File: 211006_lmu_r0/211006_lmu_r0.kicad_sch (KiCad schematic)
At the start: 17 parts, among them J1 Conn_02x03_Odd_Even, J14 Conn_01x02, J15 Conn_01x02, J16 Conn_01x02, J17 Conn_01x02, J18 Conn_01x02, J19 Conn_01x02, J2 Conn_02x03_Odd_Even, J20 Conn_01x02, J21 Conn_01x02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

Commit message: little bit closer
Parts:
- gave numbers to parts that had none: 1

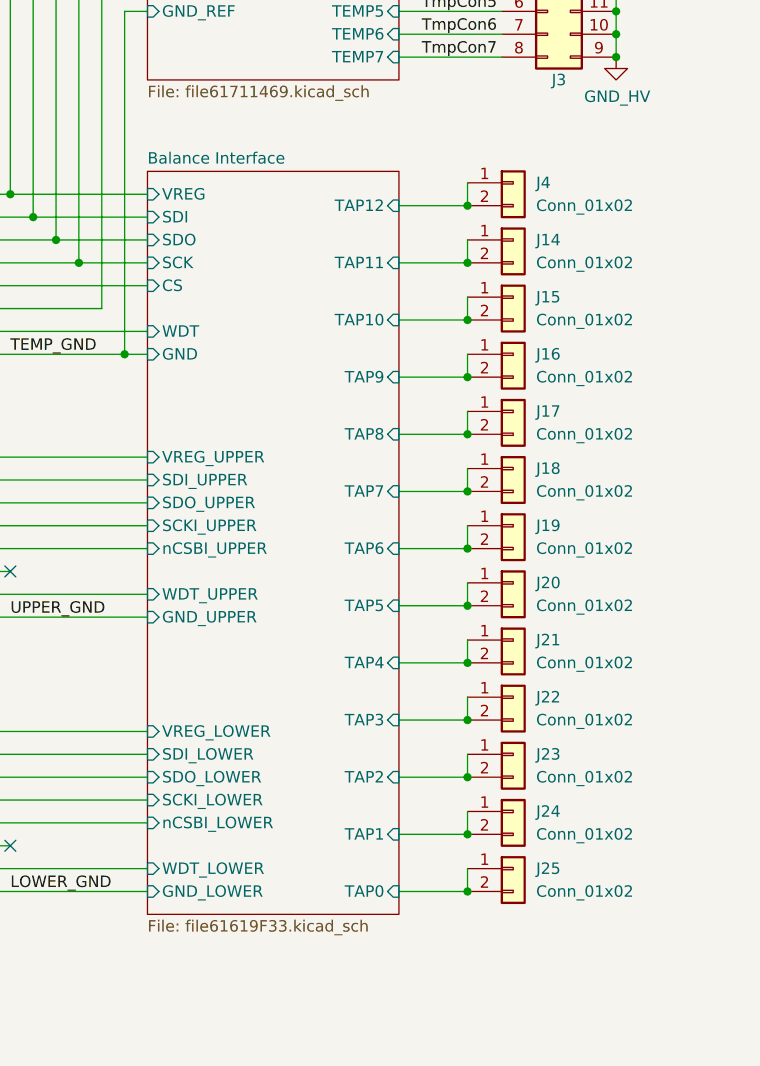
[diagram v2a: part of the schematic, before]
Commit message: sorted header location
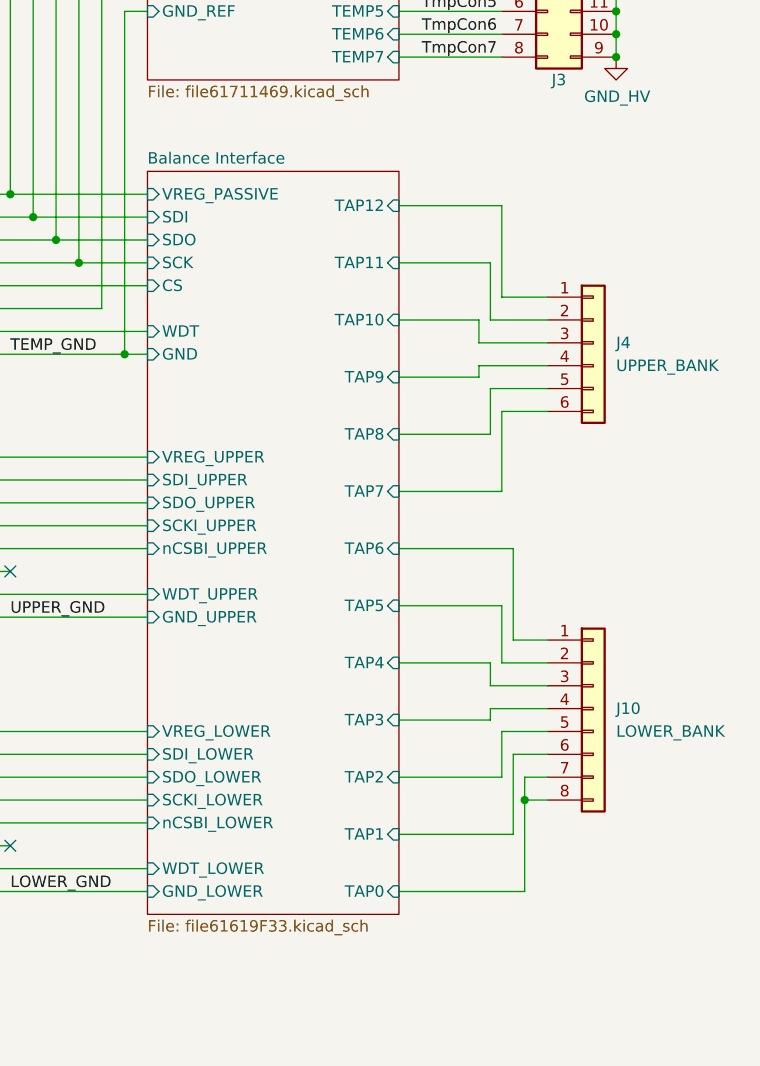
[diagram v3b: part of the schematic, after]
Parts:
- removed J14, J15, J16, J17, J18, J19, J20, J21, J22, J23, J24, J25, J4: Conn_01x02, Connector_Molex:Molex_Mini-Fit_Jr_5566-02A_2x01_P4.20mm_Vertical, symbol Connector_Generic:Conn_01x02
- added J10: LOWER_BANK, Connector_Phoenix_MSTB:PhoenixContact_MSTBVA_2,5_8-G-5,08_1x08_P5.08mm_Vertical, symbol Connector_Generic:Conn_01x08
- added J4: UPPER_BANK, Connector_Phoenix_MSTB:PhoenixContact_MSTBVA_2,5_6-G_1x06_P5.00mm_Vertical, symbol Connector_Generic:Conn_01x06
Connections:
- net Balance Interface/TAP0: now also J10.7 (Pin_7), J10.8 (Pin_8)
- net Balance Interface/TAP1: now also J10.6 (Pin_6)
- net Balance Interface/TAP10: now also J4.3 (Pin_3)
- net Balance Interface/TAP11: now also J4.2 (Pin_2)
- net Balance Interface/TAP12: now also J4.1 (Pin_1)
- net Balance Interface/TAP2: now also J10.5 (Pin_5)
- net Balance Interface/TAP3: now also J10.4 (Pin_4)
- net Balance Interface/TAP4: now also J10.3 (Pin_3)
- net Balance Interface/TAP5: now also J10.2 (Pin_2)
- net Balance Interface/TAP6: now also J10.1 (Pin_1)
- net Balance Interface/TAP7: now also J4.6 (Pin_6)
- net Balance Interface/TAP8: now also J4.5 (Pin_5)
- net Balance Interface/TAP9: now also J4.4 (Pin_4)
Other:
- sheet Balance Interface ports: added VREG_PASSIVE; removed VREG
